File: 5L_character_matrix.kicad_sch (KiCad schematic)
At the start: 14 parts, among them U1 SN74LVC244A, U2 SM411006N/15, U3 SM411006N/15, U4 SN74LVC244A, U5 SM411006N/15, U6 SM411006N/15, U7 SM411006N/15

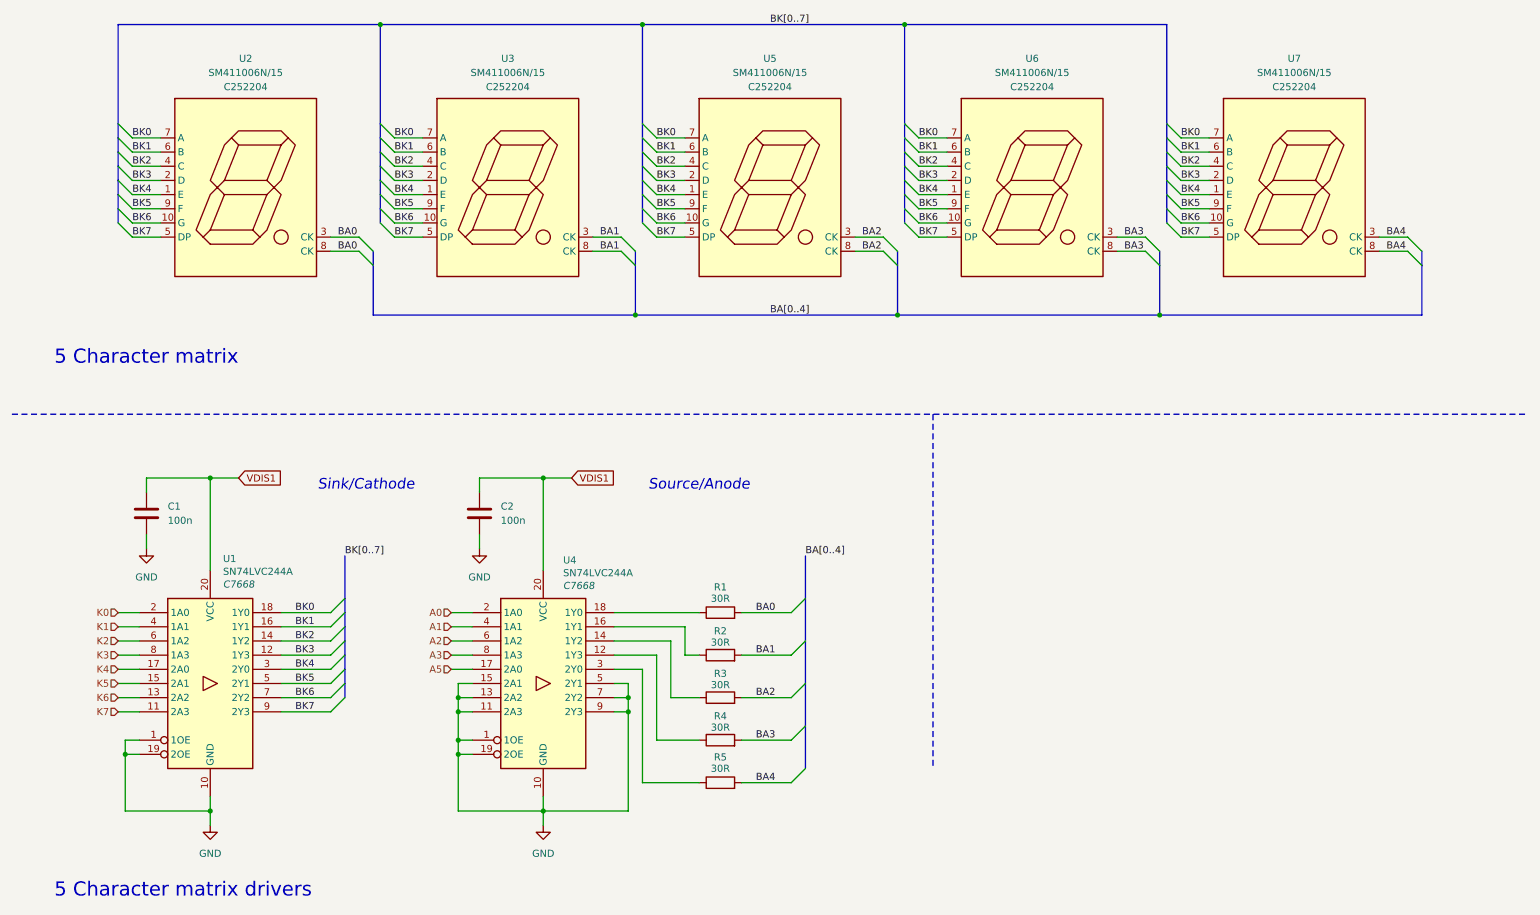
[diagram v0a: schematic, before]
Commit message: power circuit added
- addition of power circuit
- added bypassing circuit
- new formatting of the schematic
- root schematic updated
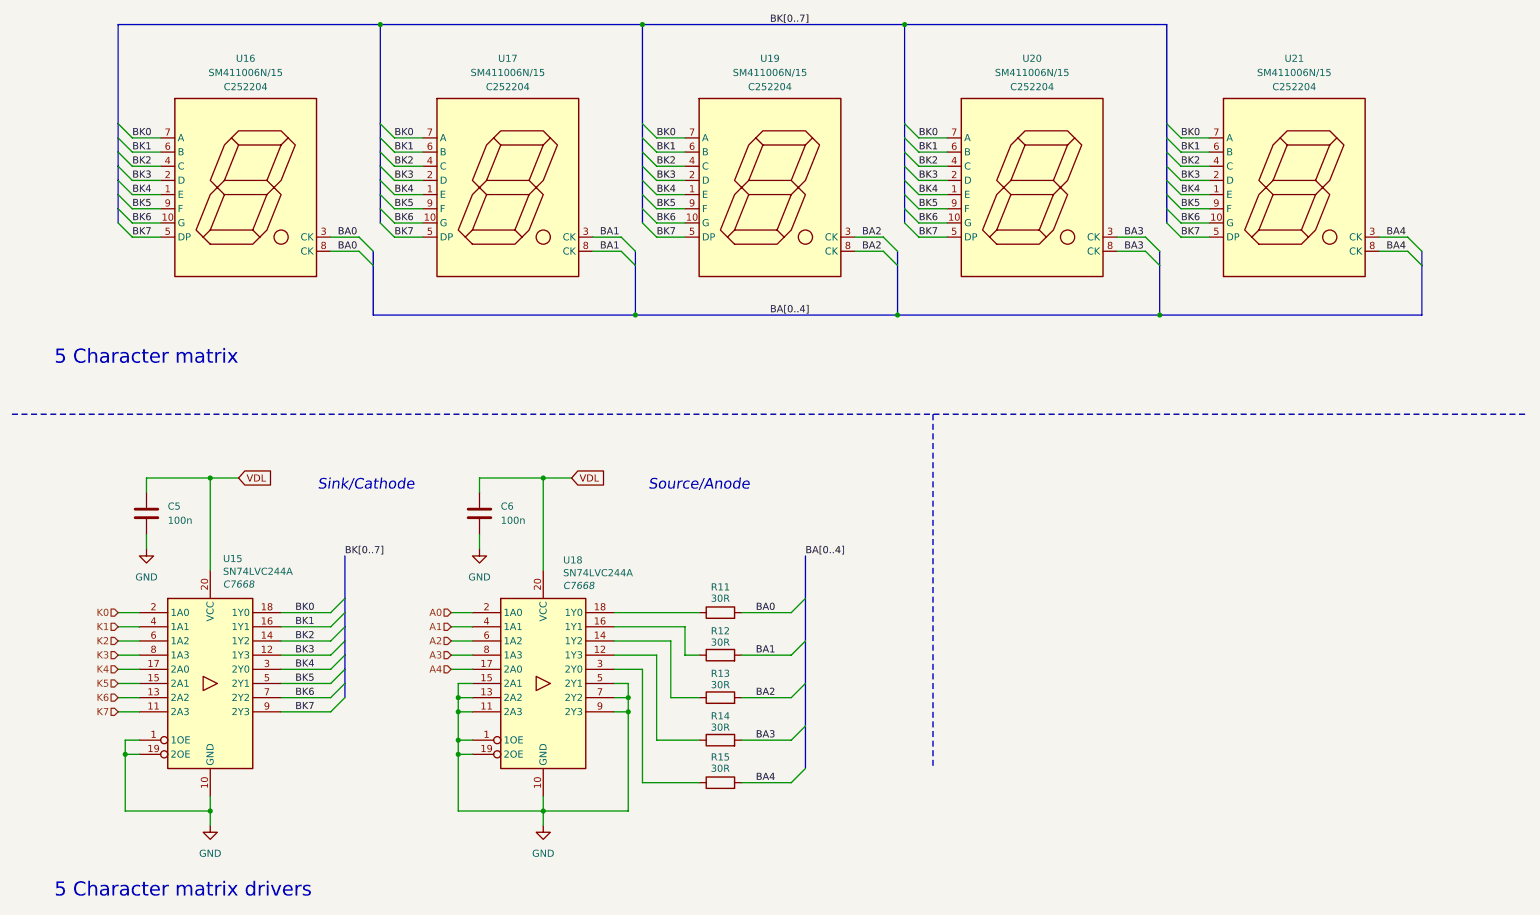
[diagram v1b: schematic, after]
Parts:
- renumbered C1 to C5, C2 to C6, R1 to R11, R2 to R12, R3 to R13, R4 to R14, R5 to R15, U1 to U15, U2 to U16, U3 to U17, U4 to U18, U5 to U19, U6 to U20, U7 to U21
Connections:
- net A5 renamed A4
- net VDIS1 renamed VDL
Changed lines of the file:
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@@
 		)
 	)
-	(global_label "VDIS1"
+	(global_label "VDL"
 		(shape input)
 		(at 113.03 113.03 0)
@@
 		)
 		(property "Intersheetrefs" "${INTERSHEET_REFS}"
-			(at 121.3976 113.03 0)
+			(at 119.4019 113.03 0)
 			(effects
 				(font
@@
 		)
 	)
-	(global_label "VDIS1"
+	(global_label "VDL"
 		(shape input)
 		(at 53.34 113.03 0)
@@
 		)
 		(property "Intersheetrefs" "${INTERSHEET_REFS}"
-			(at 61.7076 113.03 0)
+			(at 59.7119 113.03 0)
 			(effects
 				(font
@@
 		)
 	)
-	(hierarchical_label "A5"
+	(hierarchical_label "A4"
 		(shape input)
 		(at 91.44 147.32 180)
@@
 		(on_board yes)
 		(dnp no)
-		(property "Reference" "R4"
+		(property "Reference" "R14"
 			(at 139.7 155.702 90)
 			(effects
@@
 					(unit 1)
 				)
-				(path "/c9a8ff63-a0d1-4125-9dd1-40fb53daf536/95a63663-b2f9-448f-a4dd-b71321e8f379"
-					(reference "R4")
-					(unit 1)
-				)
-				(path "/c9a8ff63-a0d1-4125-9dd1-40fb53daf536/e0daf664-e239-498f-ad2e-96c4213a6fbd"
-					(reference "R9")
-					(unit 1)
-				)
 			)
 		)
@@
 		(on_board yes)
 		(dnp no)
-		(property "Reference" "U3"
+		(property "Reference" "U17"
 			(at 101.6 37.846 0)
 			(effects
@@
 					(unit 1)
 				)
-				(path "/c9a8ff63-a0d1-4125-9dd1-40fb53daf536/95a63663-b2f9-448f-a4dd-b71321e8f379"
-					(reference "U3")
-					(unit 1)
-				)
-				(path "/c9a8ff63-a0d1-4125-9dd1-40fb53daf536/e0daf664-e239-498f-ad2e-96c4213a6fbd"
-					(reference "U10")
-					(unit 1)
-				)
 			)
 		)
@@
 		(dnp no)
 		(fields_autoplaced yes)
-		(property "Reference" "C1"
+		(property "Reference" "C5"
 			(at 40.64 118.1099 0)
 			(effects
@@
 					(unit 1)
 				)
-				(path "/c9a8ff63-a0d1-4125-9dd1-40fb53daf536/95a63663-b2f9-448f-a4dd-b71321e8f379"
-					(reference "C1")
-					(unit 1)
-				)
-				(path "/c9a8ff63-a0d1-4125-9dd1-40fb53daf536/e0daf664-e239-498f-ad2e-96c4213a6fbd"
-					(reference "C3")
-					(unit 1)
-				)
 			)
 		)
@@
 		(dnp no)
 		(fields_autoplaced yes)
-		(property "Reference" "C2"
+		(property "Reference" "C6"
 			(at 100.33 118.1099 0)
 			(effects
@@
 					(unit 1)
 				)
-				(path "/c9a8ff63-a0d1-4125-9dd1-40fb53daf536/95a63663-b2f9-448f-a4dd-b71321e8f379"
-					(reference "C2")
-					(unit 1)
-				)
-				(path "/c9a8ff63-a0d1-4125-9dd1-40fb53daf536/e0daf664-e239-498f-ad2e-96c4213a6fbd"
-					(reference "C4")
-					(unit 1)
-				)
 			)
 		)
@@
 		(on_board yes)
 		(dnp no)
-		(property "Reference" "U6"
+		(property "Reference" "U20"
 			(at 195.58 37.846 0)
 			(effects
@@
 					(unit 1)
 				)
-				(path "/c9a8ff63-a0d1-4125-9dd1-40fb53daf536/95a63663-b2f9-448f-a4dd-b71321e8f379"
-					(reference "U6")
-					(unit 1)
-				)
-				(path "/c9a8ff63-a0d1-4125-9dd1-40fb53daf536/e0daf664-e239-498f-ad2e-96c4213a6fbd"
-					(reference "U13")
-					(unit 1)
-				)
 			)
 		)
@@
 		(dnp no)
 		(fields_autoplaced yes)
-		(property "Reference" "#PWR01"
+		(property "Reference" "#PWR09"
 			(at 36.83 132.08 0)
 			(effects
@@
 					(unit 1)
 				)
-				(path "/c9a8ff63-a0d1-4125-9dd1-40fb53daf536/95a63663-b2f9-448f-a4dd-b71321e8f379"
-					(reference "#PWR01")
-					(unit 1)
-				)
-				(path "/c9a8ff63-a0d1-4125-9dd1-40fb53daf536/e0daf664-e239-498f-ad2e-96c4213a6fbd"
-					(reference "#PWR05")
-					(unit 1)
-				)
 			)
 		)
@@
 		(on_board yes)
 		(dnp no)
-		(property "Reference" "R2"
+		(property "Reference" "R12"
 			(at 139.7 140.462 90)
 			(effects
@@
 					(unit 1)
 				)
-				(path "/c9a8ff63-a0d1-4125-9dd1-40fb53daf536/95a63663-b2f9-448f-a4dd-b71321e8f379"
-					(reference "R2")
-					(unit 1)
-				)
-				(path "/c9a8ff63-a0d1-4125-9dd1-40fb53daf536/e0daf664-e239-498f-ad2e-96c4213a6fbd"
-					(reference "R7")
-					(unit 1)
-				)
 			)
 		)
@@
 		(on_board yes)
 		(dnp no)
-		(property "Reference" "U5"
+		(property "Reference" "U19"
 			(at 148.59 37.846 0)
 			(effects
@@
 					(unit 1)
 				)
-				(path "/c9a8ff63-a0d1-4125-9dd1-40fb53daf536/95a63663-b2f9-448f-a4dd-b71321e8f379"
-					(reference "U5")
-					(unit 1)
-				)
-				(path "/c9a8ff63-a0d1-4125-9dd1-40fb53daf536/e0daf664-e239-498f-ad2e-96c4213a6fbd"
-					(reference "U12")
-					(unit 1)
-				)
 			)
 		)
@@
 		(on_board yes)
 		(dnp no)
-		(property "Reference" "U1"
+		(property "Reference" "U15"
 			(at 50.546 127.508 0)
 			(effects
@@
 					(unit 1)
 				)
-				(path "/c9a8ff63-a0d1-4125-9dd1-40fb53daf536/95a63663-b2f9-448f-a4dd-b71321e8f379"
-					(reference "U1")
-					(unit 1)
-				)
-				(path "/c9a8ff63-a0d1-4125-9dd1-40fb53daf536/e0daf664-e239-498f-ad2e-96c4213a6fbd"
-					(reference "U8")
-					(unit 1)
-				)
 			)
 		)
@@
 		(dnp no)
 		(fields_autoplaced yes)
-		(property "Reference" "#PWR03"
+		(property "Reference" "#PWR011"
 			(at 96.52 132.08 0)
 			(effects
@@
 					(unit 1)
 				)
-				(path "/c9a8ff63-a0d1-4125-9dd1-40fb53daf536/95a63663-b2f9-448f-a4dd-b71321e8f379"
-					(reference "#PWR03")
-					(unit 1)
-				)
-				(path "/c9a8ff63-a0d1-4125-9dd1-40fb53daf536/e0daf664-e239-498f-ad2e-96c4213a6fbd"
-					(reference "#PWR07")
-					(unit 1)
-				)
 			)
 		)
@@
 		(on_board yes)
 		(dnp no)
-		(property "Reference" "U4"
+		(property "Reference" "U18"
 			(at 111.506 127.762 0)
 			(effects
@@
 					(unit 1)
 				)
-				(path "/c9a8ff63-a0d1-4125-9dd1-40fb53daf536/95a63663-b2f9-448f-a4dd-b71321e8f379"
-					(reference "U4")
-					(unit 1)
-				)
-				(path "/c9a8ff63-a0d1-4125-9dd1-40fb53daf536/e0daf664-e239-498f-ad2e-96c4213a6fbd"
-					(reference "U11")
-					(unit 1)
-				)
 			)
 		)
@@
 		(dnp no)
 		(fields_autoplaced yes)
-		(property "Reference" "#PWR02"
+		(property "Reference" "#PWR010"
 			(at 48.26 181.61 0)
 			(effects
@@
 					(unit 1)
 				)
-				(path "/c9a8ff63-a0d1-4125-9dd1-40fb53daf536/95a63663-b2f9-448f-a4dd-b71321e8f379"
-					(reference "#PWR02")
-					(unit 1)
-				)
-				(path "/c9a8ff63-a0d1-4125-9dd1-40fb53daf536/e0daf664-e239-498f-ad2e-96c4213a6fbd"
-					(reference "#PWR06")
-					(unit 1)
-				)
 			)
 		)
@@
 		(on_board yes)
 		(dnp no)
-		(property "Reference" "U2"
+		(property "Reference" "U16"
 			(at 54.61 37.846 0)
 			(effects
@@
 		)
 		(instances
-			(project ""
+			(project "Precision Clock"
 				(path "/c9a8ff63-a0d1-4125-9dd1-40fb53daf536/61b252ee-6ab4-4417-a4ad-7fc052d7ca20"
 					(reference "U16")
-					(unit 1)
-				)
-				(path "/c9a8ff63-a0d1-4125-9dd1-40fb53daf536/95a63663-b2f9-448f-a4dd-b71321e8f379"
-					(reference "U2")
-					(unit 1)
-				)
-				(path "/c9a8ff63-a0d1-4125-9dd1-40fb53daf536/e0daf664-e239-498f-ad2e-96c4213a6fbd"
-					(reference "U9")
 					(unit 1)
 				)
@@
 		(on_board yes)
 		(dnp no)
-		(property "Reference" "R5"
+		(property "Reference" "R15"
 			(at 139.7 163.068 90)
 			(effects
@@
 					(unit 1)
 				)
-				(path "/c9a8ff63-a0d1-4125-9dd1-40fb53daf536/95a63663-b2f9-448f-a4dd-b71321e8f379"
-					(reference "R5")
-					(unit 1)
-				)
-				(path "/c9a8ff63-a0d1-4125-9dd1-40fb53daf536/e0daf664-e239-498f-ad2e-96c4213a6fbd"
-					(reference "R10")
-					(unit 1)
-				)
 			)
 		)
@@
 		(dnp no)
 		(fields_autoplaced yes)
-		(property "Reference" "#PWR04"
+		(property "Reference" "#PWR012"
 			(at 107.95 181.61 0)
 			(effects
@@
 					(unit 1)
 				)
-				(path "/c9a8ff63-a0d1-4125-9dd1-40fb53daf536/95a63663-b2f9-448f-a4dd-b71321e8f379"
-					(reference "#PWR04")
-					(unit 1)
-				)
-				(path "/c9a8ff63-a0d1-4125-9dd1-40fb53daf536/e0daf664-e239-498f-ad2e-96c4213a6fbd"
-					(reference "#PWR08")
-					(unit 1)
-				)
 			)
 		)
@@
 		(on_board yes)
 		(dnp no)
-		(property "Reference" "U7"
+		(property "Reference" "U21"
 			(at 242.57 37.846 0)
 			(effects
@@
 					(unit 1)
 				)
-				(path "/c9a8ff63-a0d1-4125-9dd1-40fb53daf536/95a63663-b2f9-448f-a4dd-b71321e8f379"
-					(reference "U7")
-					(unit 1)
-				)
-				(path "/c9a8ff63-a0d1-4125-9dd1-40fb53daf536/e0daf664-e239-498f-ad2e-96c4213a6fbd"
-					(reference "U14")
-					(unit 1)
-				)
 			)
 		)
@@
 		(on_board yes)
 		(dnp no)
-		(property "Reference" "R1"
+		(property "Reference" "R11"
 			(at 139.7 132.588 90)
 			(effects
@@
 					(unit 1)
 				)
-				(path "/c9a8ff63-a0d1-4125-9dd1-40fb53daf536/95a63663-b2f9-448f-a4dd-b71321e8f379"
-					(reference "R1")
-					(unit 1)
-				)
-				(path "/c9a8ff63-a0d1-4125-9dd1-40fb53daf536/e0daf664-e239-498f-ad2e-96c4213a6fbd"
-					(reference "R6")
-					(unit 1)
-				)
 			)
 		)
@@
 		(on_board yes)
 		(dnp no)
-		(property "Reference" "R3"
+		(property "Reference" "R13"
 			(at 139.7 148.082 90)
 			(effects
@@
 					(unit 1)
 				)
-				(path "/c9a8ff63-a0d1-4125-9dd1-40fb53daf536/95a63663-b2f9-448f-a4dd-b71321e8f379"
-					(reference "R3")
-					(unit 1)
-				)
-				(path "/c9a8ff63-a0d1-4125-9dd1-40fb53daf536/e0daf664-e239-498f-ad2e-96c4213a6fbd"
-					(reference "R8")
-					(unit 1)
-				)
